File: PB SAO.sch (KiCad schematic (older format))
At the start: 9 parts, among them J1 SAO_F, J2 SAO_F, Q1 2N7002, SW1 SW_Push

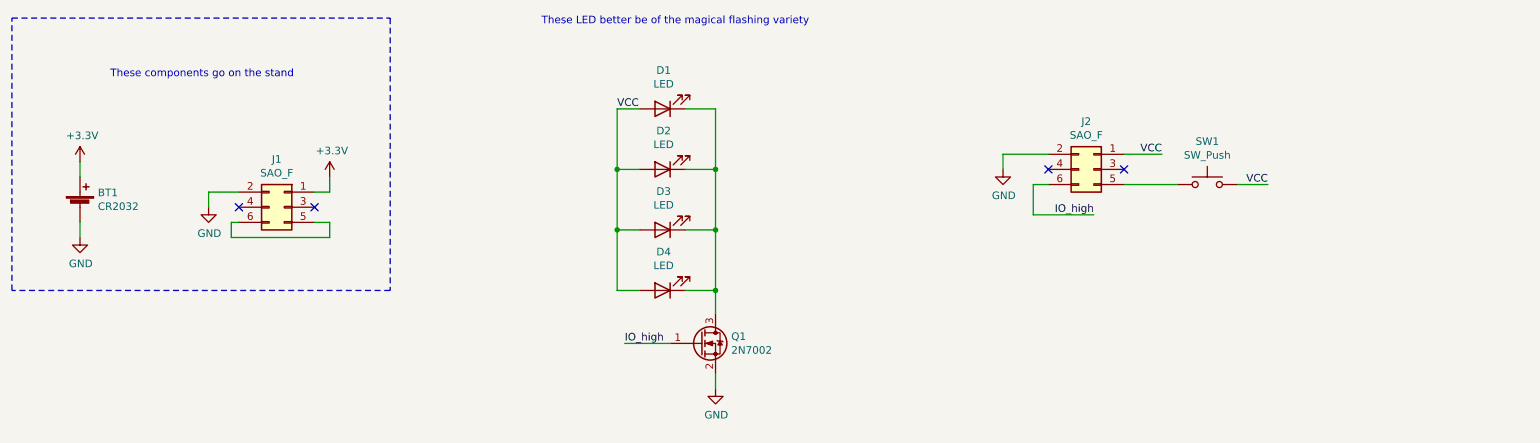
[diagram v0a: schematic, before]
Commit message: Updated footprints
Dual footprints.
Updated edge cuts
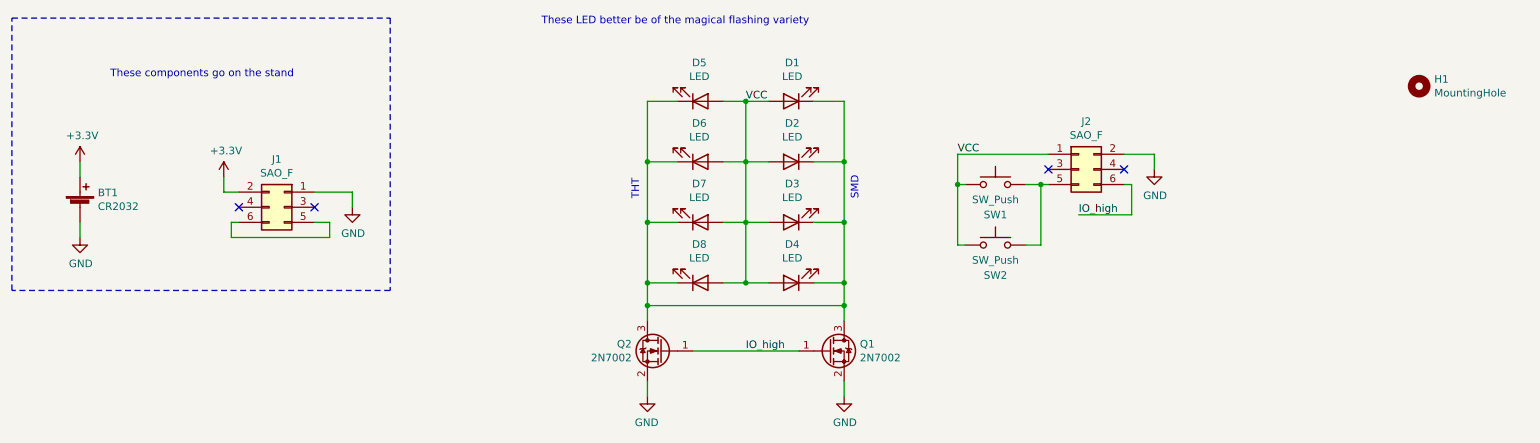
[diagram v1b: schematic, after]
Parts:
- added D5, D6, D7, D8: LED, LED_THT:LED_D3.0mm, symbol Device:LED
- added H1: MountingHole, MountingHole:MountingHole_3mm, symbol Mechanical:MountingHole
- added Q2: 2N7002, Package_TO_SOT_THT:TO-92, symbol Transistor_FET:2N7002
- added SW2: SW_Push, Button_Switch_SMD:SW_Push_1P1T_NO_6x6mm_H9.5mm, symbol Switch:SW_Push
- BT1: footprint (none) -> Battery:BatteryHolder_Keystone_3034_1x20mm
- D1, D2, D3, D4: footprint (none) -> LED_SMD:LED_0805_2012Metric_Pad1.15x1.40mm_HandSolder
- J1, J2: footprint (none) -> Connector_PinHeader_2.54mm:PinHeader_2x03_P2.54mm_Vertical
- Q1: footprint Package_TO_SOT_SMD:SOT-23 -> Package_TO_SOT_SMD:SOT-23_Handsoldering
- SW1: footprint (none) -> Button_Switch_THT:SW_PUSH_6mm
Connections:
- net +3V3: now also J1.2 (Pin_2); no longer J1.1 (Pin_1)
- net GND: now also J1.1 (Pin_1), Q2.2 (S); no longer J1.2 (Pin_2)
- net IO_high: now also Q2.1 (G)
- net VCC: now also SW1.1, D5.2 (A), D6.2 (A), D7.2 (A), D8.2 (A), SW2.1; no longer SW1.2
- net at D1.1 (K), D2.1 (K), D3.1 (K)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: now also D5.1 (K), D6.1 (K), D7.1 (K), D8.1 (K), Q2.3 (D)
- net at J2.5 (Pin_5): now also SW1.2, SW2.2; no longer SW1.1
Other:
- note added: "SMD"
- note added: "THT"
- moved on the sheet: D1, D2, D3, D4, Q1, SW1
